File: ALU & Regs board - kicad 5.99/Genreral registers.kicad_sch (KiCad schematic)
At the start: 32 parts, among them U29 MC74ACT374DWG, U30 MC74ACT374DWG, U31 MC74ACT374DWG, U32 MC74ACT374DWG, U33 MC74ACT374DWG, U34 MC74ACT374DWG, U35 MC74ACT374DWG, U36 MC74ACT374DWG, U37 MC74ACT374DWG, U38 MC74ACT374DWG, U39 MC74ACT374DWG, U40 MC74ACT374DWG, U41 MC74ACT374DWG, U42 MC74ACT374DWG, U43 MC74ACT374DWG, U44 MC74ACT374DWG

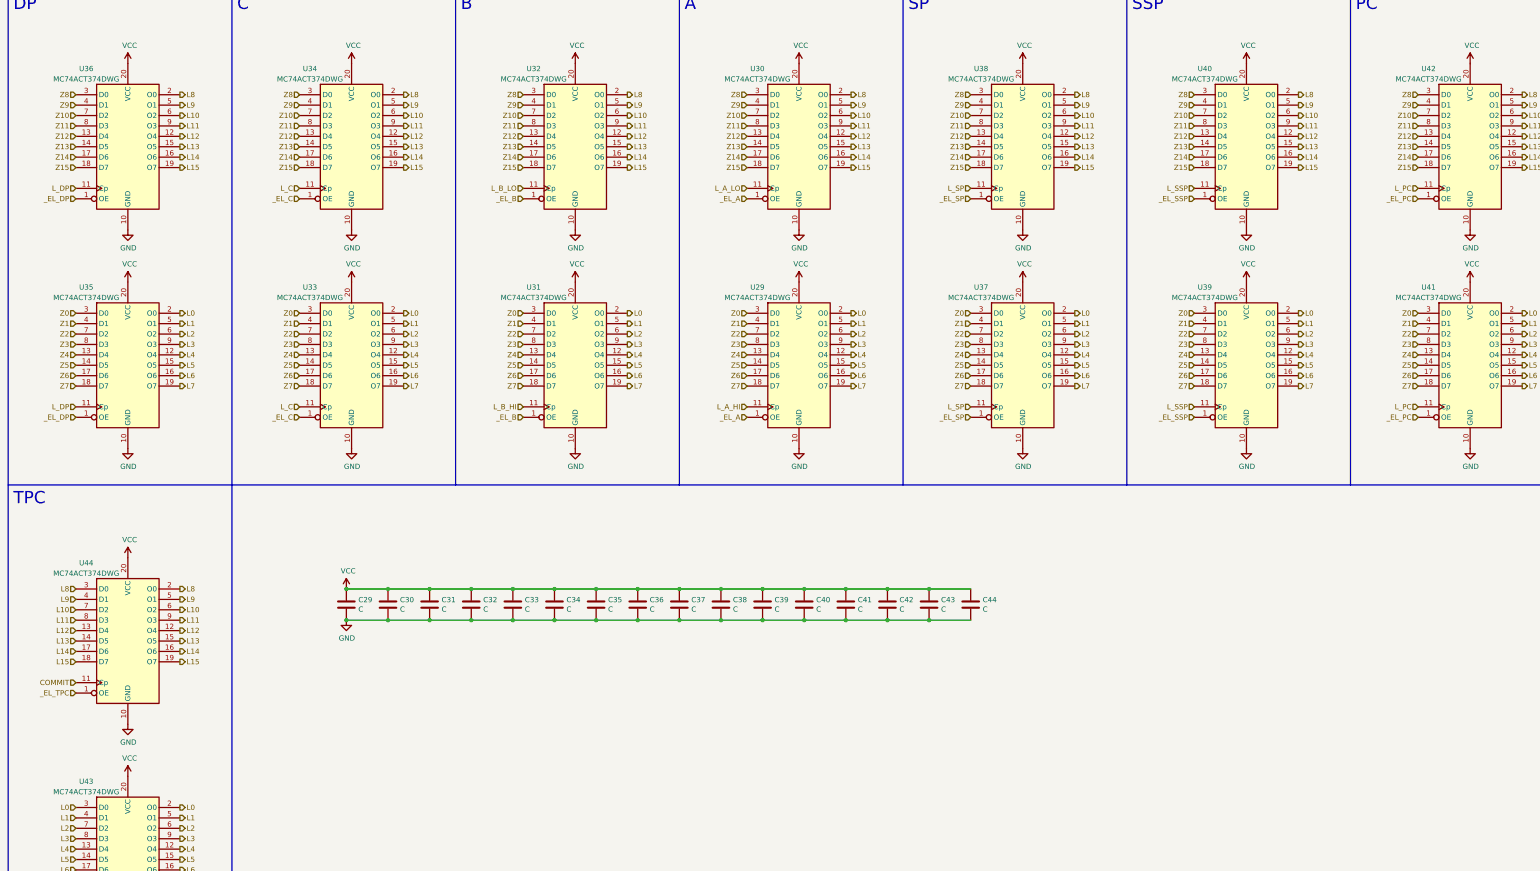
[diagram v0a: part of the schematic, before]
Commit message: added a buffer on the _RESET line, which is rather loaded
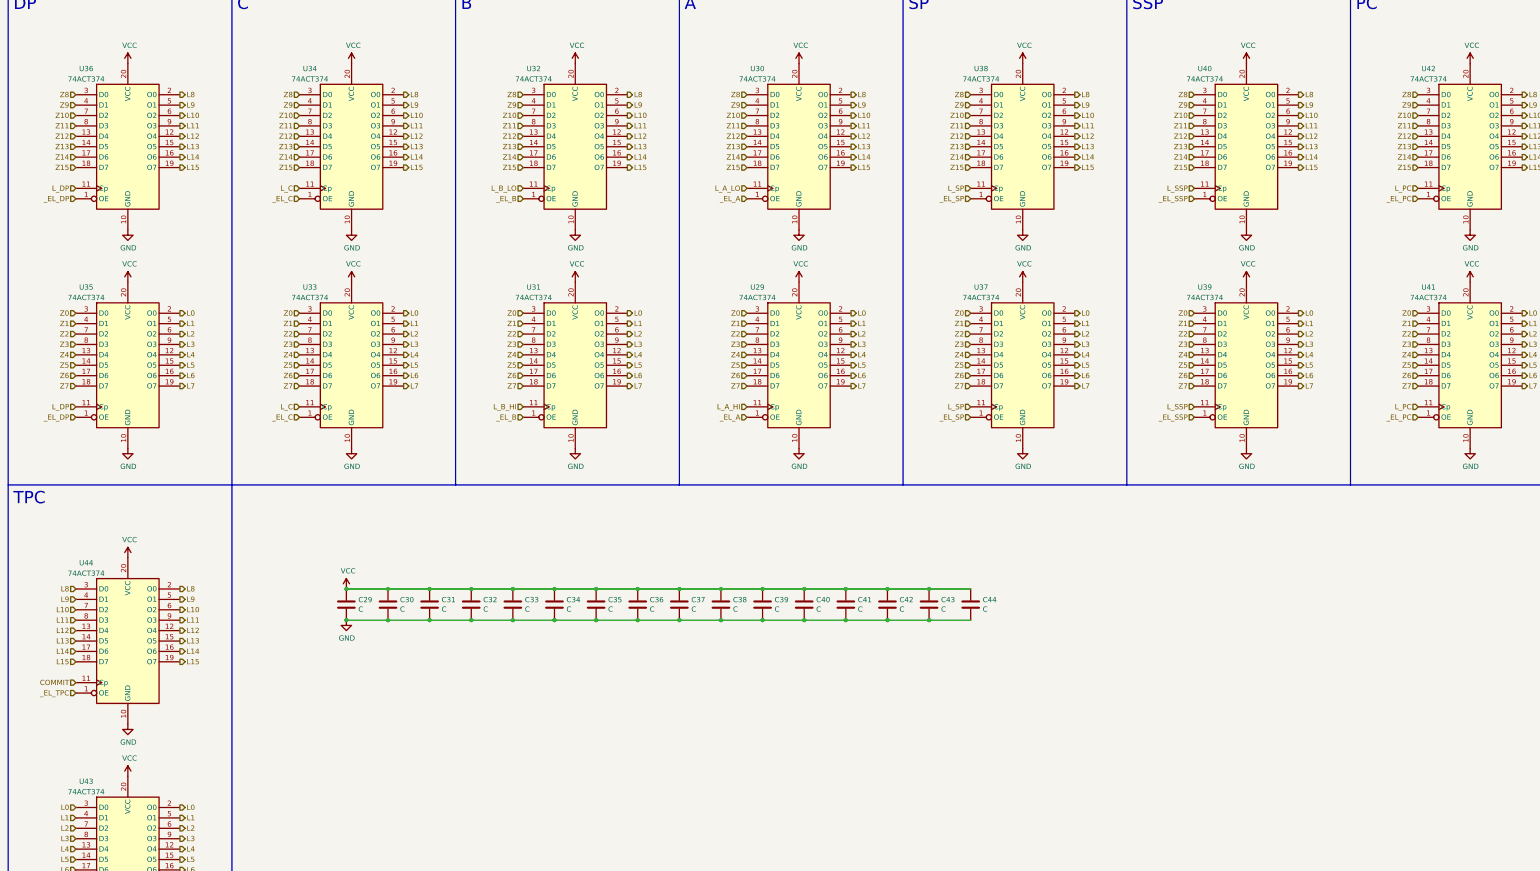
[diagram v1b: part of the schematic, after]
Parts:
- U29, U30, U31, U32, U33, U34, U35, U36, U37, U38, U39, U40, U41, U42, U43, U44: value MC74ACT374DWG -> 74ACT374
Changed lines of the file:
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@@
     (in_bom yes) (on_board yes)
     (property "Reference" "U36" (id 0) (at 35.56 36.83 0))
-    (property "Value" "MC74ACT374DWG " (id 1) (at 35.56 39.37 0))
+    (property "Value" "74ACT374" (id 1) (at 35.56 39.37 0))
     (property "Footprint" "Package_SO:SOIC-20W_7.5x12.8mm_P1.27mm" (id 2) (at 45.72 55.88 0)
       (effects (font (size 1.27 1.27)) hide)
@@
     (in_bom yes) (on_board yes)
     (property "Reference" "U35" (id 0) (at 35.56 90.17 0))
-    (property "Value" "MC74ACT374DWG " (id 1) (at 35.56 92.71 0))
+    (property "Value" "74ACT374" (id 1) (at 35.56 92.71 0))
     (property "Footprint" "Package_SO:SOIC-20W_7.5x12.8mm_P1.27mm" (id 2) (at 45.72 109.22 0)
       (effects (font (size 1.27 1.27)) hide)
@@
     (in_bom yes) (on_board yes)
     (property "Reference" "U44" (id 0) (at 35.56 157.48 0))
-    (property "Value" "MC74ACT374DWG " (id 1) (at 35.56 160.02 0))
+    (property "Value" "74ACT374" (id 1) (at 35.56 160.02 0))
     (property "Footprint" "Package_SO:SOIC-20W_7.5x12.8mm_P1.27mm" (id 2) (at 45.72 176.53 0)
       (effects (font (size 1.27 1.27)) hide)
@@
     (in_bom yes) (on_board yes)
     (property "Reference" "U43" (id 0) (at 35.56 210.82 0))
-    (property "Value" "MC74ACT374DWG " (id 1) (at 35.56 213.36 0))
+    (property "Value" "74ACT374" (id 1) (at 35.56 213.36 0))
     (property "Footprint" "Package_SO:SOIC-20W_7.5x12.8mm_P1.27mm" (id 2) (at 45.72 229.87 0)
       (effects (font (size 1.27 1.27)) hide)
@@
     (in_bom yes) (on_board yes)
     (property "Reference" "U34" (id 0) (at 90.17 36.83 0))
-    (property "Value" "MC74ACT374DWG " (id 1) (at 90.17 39.37 0))
+    (property "Value" "74ACT374" (id 1) (at 90.17 39.37 0))
     (property "Footprint" "Package_SO:SOIC-20W_7.5x12.8mm_P1.27mm" (id 2) (at 100.33 55.88 0)
       (effects (font (size 1.27 1.27)) hide)
@@
     (in_bom yes) (on_board yes)
     (property "Reference" "U33" (id 0) (at 90.17 90.17 0))
-    (property "Value" "MC74ACT374DWG " (id 1) (at 90.17 92.71 0))
+    (property "Value" "74ACT374" (id 1) (at 90.17 92.71 0))
     (property "Footprint" "Package_SO:SOIC-20W_7.5x12.8mm_P1.27mm" (id 2) (at 100.33 109.22 0)
       (effects (font (size 1.27 1.27)) hide)
@@
     (in_bom yes) (on_board yes)
     (property "Reference" "U32" (id 0) (at 144.78 36.83 0))
-    (property "Value" "MC74ACT374DWG " (id 1) (at 144.78 39.37 0))
+    (property "Value" "74ACT374" (id 1) (at 144.78 39.37 0))
     (property "Footprint" "Package_SO:SOIC-20W_7.5x12.8mm_P1.27mm" (id 2) (at 154.94 55.88 0)
       (effects (font (size 1.27 1.27)) hide)
@@
     (in_bom yes) (on_board yes)
     (property "Reference" "U31" (id 0) (at 144.78 90.17 0))
-    (property "Value" "MC74ACT374DWG " (id 1) (at 144.78 92.71 0))
+    (property "Value" "74ACT374" (id 1) (at 144.78 92.71 0))
     (property "Footprint" "Package_SO:SOIC-20W_7.5x12.8mm_P1.27mm" (id 2) (at 154.94 109.22 0)
       (effects (font (size 1.27 1.27)) hide)
@@
     (in_bom yes) (on_board yes)
     (property "Reference" "U30" (id 0) (at 199.39 36.83 0))
-    (property "Value" "MC74ACT374DWG " (id 1) (at 199.39 39.37 0))
+    (property "Value" "74ACT374" (id 1) (at 199.39 39.37 0))
     (property "Footprint" "Package_SO:SOIC-20W_7.5x12.8mm_P1.27mm" (id 2) (at 209.55 55.88 0)
       (effects (font (size 1.27 1.27)) hide)
@@
     (in_bom yes) (on_board yes)
     (property "Reference" "U29" (id 0) (at 199.39 90.17 0))
-    (property "Value" "MC74ACT374DWG " (id 1) (at 199.39 92.71 0))
+    (property "Value" "74ACT374" (id 1) (at 199.39 92.71 0))
     (property "Footprint" "Package_SO:SOIC-20W_7.5x12.8mm_P1.27mm" (id 2) (at 209.55 109.22 0)
       (effects (font (size 1.27 1.27)) hide)
@@
     (in_bom yes) (on_board yes)
     (property "Reference" "U38" (id 0) (at 254 36.83 0))
-    (property "Value" "MC74ACT374DWG " (id 1) (at 254 39.37 0))
+    (property "Value" "74ACT374" (id 1) (at 254 39.37 0))
     (property "Footprint" "Package_SO:SOIC-20W_7.5x12.8mm_P1.27mm" (id 2) (at 264.16 55.88 0)
       (effects (font (size 1.27 1.27)) hide)
@@
     (in_bom yes) (on_board yes)
     (property "Reference" "U37" (id 0) (at 254 90.17 0))
-    (property "Value" "MC74ACT374DWG " (id 1) (at 254 92.71 0))
+    (property "Value" "74ACT374" (id 1) (at 254 92.71 0))
     (property "Footprint" "Package_SO:SOIC-20W_7.5x12.8mm_P1.27mm" (id 2) (at 264.16 109.22 0)
       (effects (font (size 1.27 1.27)) hide)
@@
     (in_bom yes) (on_board yes)
     (property "Reference" "U40" (id 0) (at 308.61 36.83 0))
-    (property "Value" "MC74ACT374DWG " (id 1) (at 308.61 39.37 0))
+    (property "Value" "74ACT374" (id 1) (at 308.61 39.37 0))
     (property "Footprint" "Package_SO:SOIC-20W_7.5x12.8mm_P1.27mm" (id 2) (at 318.77 55.88 0)
       (effects (font (size 1.27 1.27)) hide)
@@
     (in_bom yes) (on_board yes)
     (property "Reference" "U39" (id 0) (at 308.61 90.17 0))
-    (property "Value" "MC74ACT374DWG " (id 1) (at 308.61 92.71 0))
+    (property "Value" "74ACT374" (id 1) (at 308.61 92.71 0))
     (property "Footprint" "Package_SO:SOIC-20W_7.5x12.8mm_P1.27mm" (id 2) (at 318.77 109.22 0)
       (effects (font (size 1.27 1.27)) hide)
@@
     (in_bom yes) (on_board yes)
     (property "Reference" "U42" (id 0) (at 363.22 36.83 0))
-    (property "Value" "MC74ACT374DWG " (id 1) (at 363.22 39.37 0))
+    (property "Value" "74ACT374" (id 1) (at 363.22 39.37 0))
     (property "Footprint" "Package_SO:SOIC-20W_7.5x12.8mm_P1.27mm" (id 2) (at 373.38 55.88 0)
       (effects (font (size 1.27 1.27)) hide)
@@
     (in_bom yes) (on_board yes)
     (property "Reference" "U41" (id 0) (at 363.22 90.17 0))
-    (property "Value" "MC74ACT374DWG " (id 1) (at 363.22 92.71 0))
+    (property "Value" "74ACT374" (id 1) (at 363.22 92.71 0))
     (property "Footprint" "Package_SO:SOIC-20W_7.5x12.8mm_P1.27mm" (id 2) (at 373.38 109.22 0)
       (effects (font (size 1.27 1.27)) hide)
